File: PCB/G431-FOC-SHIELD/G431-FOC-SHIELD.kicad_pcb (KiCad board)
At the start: 2 copper layers, 70 x 59 mm, 2 parts, among them CN10 Conn_02x19_Odd_Even, CN7 Conn_02x19_Odd_Even

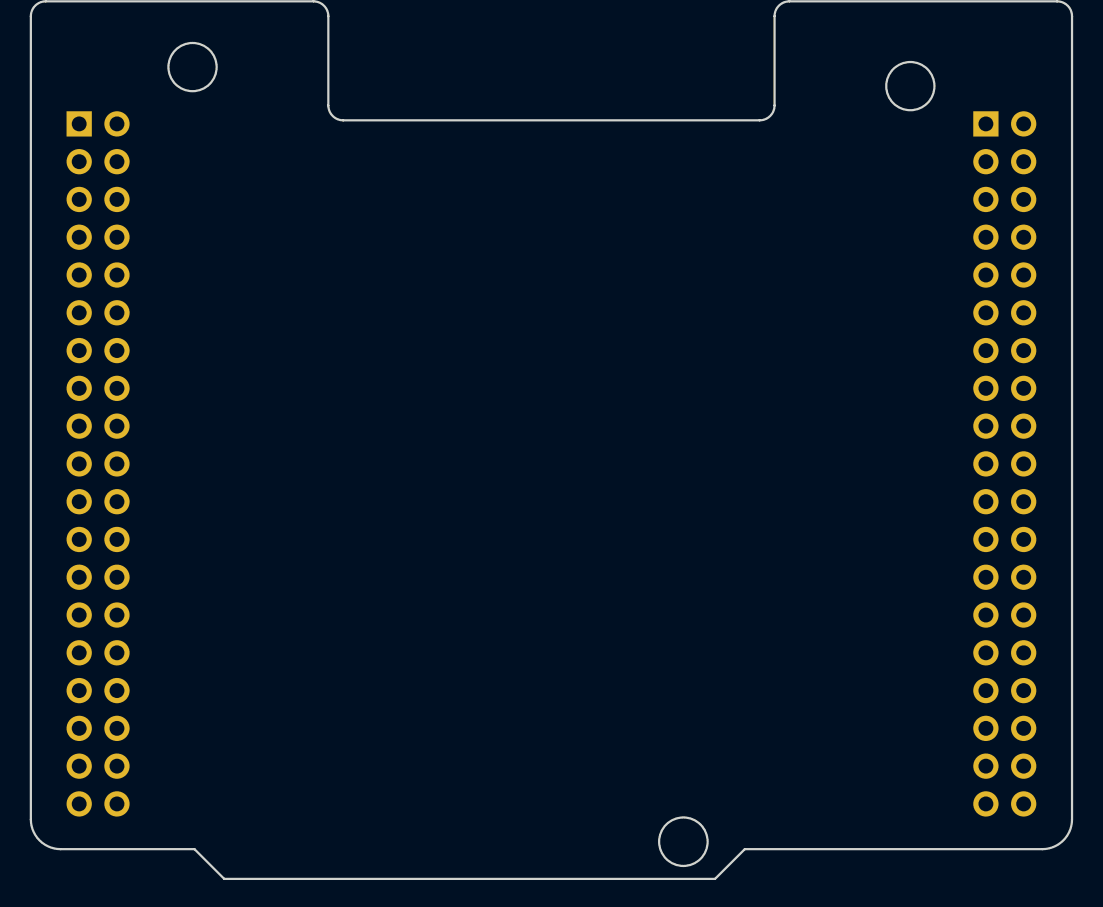
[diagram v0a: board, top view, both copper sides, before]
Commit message: started schematic design, added DRV8323 typical application
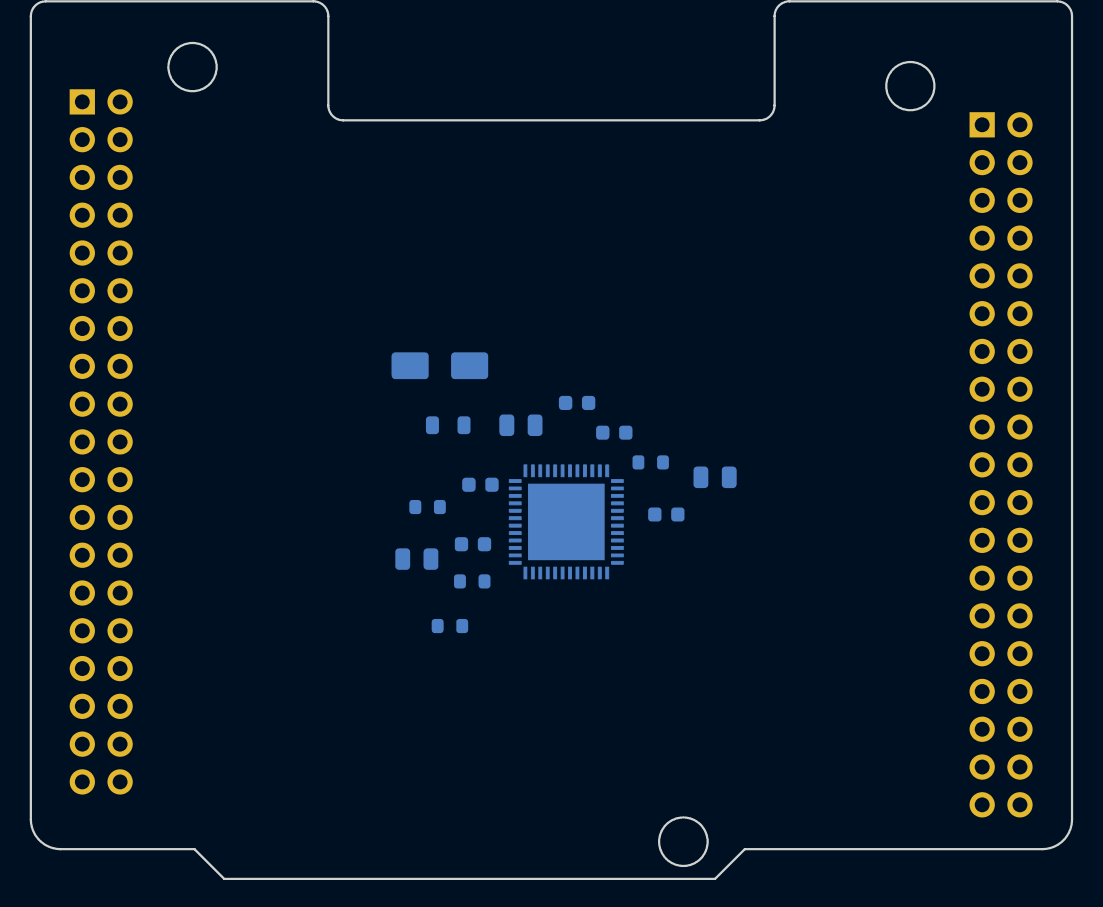
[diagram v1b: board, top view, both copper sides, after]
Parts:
- added C1: 0.1u, Capacitor_SMD:C_0603_1608Metric, B.Cu at (166.7, 90.0)
- added C2: Cin, Capacitor_SMD:C_0805_2012Metric, B.Cu at (162.9, 91.5)
- added C3: C_OUT, Capacitor_SMD:C_0805_2012Metric, B.Cu at (155.9, 100.5)
- added C4: 47u, Capacitor_SMD:C_0805_2012Metric, B.Cu at (176.0, 95.0)
- added C5: 1u, Capacitor_SMD:C_0603_1608Metric, B.Cu at (172.7, 97.5)
- added C6: 0.1u, Capacitor_SMD:C_0603_1608Metric, B.Cu at (169.2, 92.0)
- added C7: 1u, Capacitor_SMD:C_0603_1608Metric, B.Cu at (159.7, 99.5)
- added C8: 1u, Capacitor_SMD:C_0603_1608Metric, B.Cu at (160.2, 95.5)
- added D1: D_Schottky, Diode_SMD:D_SMA, B.Cu at (157.5, 87.5)
- added L1: L_OUT, Inductor_SMD:L_0805_2012Metric, B.Cu at (158.1, 91.5)
- added R1: R, Resistor_SMD:R_0603_1608Metric, B.Cu at (171.7, 94.0)
- added R2: R_FB_1, Resistor_SMD:R_0603_1608Metric, B.Cu at (159.7, 102.0)
- added R3: R_FB_2, Resistor_SMD:R_0603_1608Metric, B.Cu at (158.2, 105.0)
- added R4: 10k, Resistor_SMD:R_0603_1608Metric, B.Cu at (156.7, 97.0)
- added U1: DRV8323RSRGZR, DRV8323RSRGZR:QFN50P700X700X100-49N, B.Cu at (166.0, 98.0)
- moved CN7 1.49 mm to (133.5, 69.8)
- moved CN10 0.26 mm to (194.0, 71.3)
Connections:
- net Net-(CN10-Pad1) renamed /PC9
- net Net-(CN10-Pad11) renamed /PA5
- net Net-(CN10-Pad12) renamed /PA12
- net Net-(CN10-Pad13) renamed /PA6
- net Net-(CN10-Pad14) renamed /PA11
- net Net-(CN10-Pad15) renamed /PA7
- net Net-(CN10-Pad16) renamed /PB12
- net Net-(CN10-Pad17) renamed /PB6
- net Net-(CN10-Pad18) renamed /PB11
- net Net-(CN10-Pad19) renamed /PC7
- net Net-(CN10-Pad2) renamed /PC8
- net Net-(CN10-Pad21) renamed /PA9
- net Net-(CN10-Pad22) renamed /PB2
- net Net-(CN10-Pad23) renamed /PA8
- net Net-(CN10-Pad24) renamed /PB1
- net Net-(CN10-Pad25) renamed /PB10
- net Net-(CN10-Pad26) renamed /PB15
- net Net-(CN10-Pad27) renamed /PB4
- net Net-(CN10-Pad28) renamed /PB14
- net Net-(CN10-Pad29) renamed /PB5
- net Net-(CN10-Pad3) renamed /PB8
- net Net-(CN10-Pad30) renamed /PB13
- net Net-(CN10-Pad31) renamed /PB3
- net Net-(CN10-Pad32) renamed /AGND
- net Net-(CN10-Pad33) renamed /PA10
- net Net-(CN10-Pad34) renamed /PC4
- net Net-(CN10-Pad35) renamed /PC4/PA2
- net Net-(CN10-Pad37) renamed /PC5/PA3
- net Net-(CN10-Pad4) renamed /PC6
- net Net-(CN10-Pad5) renamed /PB9
- net Net-(CN10-Pad6) renamed /PC5
- net Net-(CN10-Pad7) renamed /AVDD
- net Net-(CN10-Pad8) renamed /5V_USB_CHGR
- net Net-(CN7-Pad1) renamed /PC10
- net Net-(CN7-Pad12) renamed /IOREF
- net Net-(CN7-Pad13) renamed /PA13
- net Net-(CN7-Pad14) renamed /NRST
- net Net-(CN7-Pad15) renamed /PA14
- net Net-(CN7-Pad16) renamed /+3V3
- net Net-(CN7-Pad17) renamed /PA15
- net Net-(CN7-Pad18) renamed /+5V
- net Net-(CN7-Pad2) renamed /PC11
- net Net-(CN7-Pad21) renamed /PB7
- net Net-(CN7-Pad23) renamed /PC13
- net Net-(CN7-Pad24) renamed /VIN
- net Net-(CN7-Pad25) renamed /PC14
- net Net-(CN7-Pad27) renamed /PC15
- net Net-(CN7-Pad28) renamed /PA0
- net Net-(CN7-Pad29) renamed /PF0
- net Net-(CN7-Pad3) renamed /PC12
- net Net-(CN7-Pad30) renamed /PA1
- net Net-(CN7-Pad31) renamed /PF1
- net Net-(CN7-Pad32) renamed /PA4
- net Net-(CN7-Pad33) renamed /VBAT
- net Net-(CN7-Pad34) renamed /PB0
- net Net-(CN7-Pad35) renamed /PC2
- net Net-(CN7-Pad36) renamed /PC1/PB9
- net Net-(CN7-Pad37) renamed /PC3
- net Net-(CN7-Pad38) renamed /PC0/PA15
- net Net-(CN7-Pad4) renamed /PD2
- net Net-(CN7-Pad5) renamed /VDD
- net Net-(CN7-Pad6) renamed /E5V
- net Net-(CN7-Pad7) renamed /PB8-BOOT0
- CN10 pad 10: Net-(CN10-Pad10) -> unconnected-(CN10-Pin_10-Pad10)
- CN10 pad 20: Net-(CN10-Pad20) -> GND
- CN10 pad 36: Net-(CN10-Pad36) -> unconnected-(CN10-Pin_36-Pad36)
- CN10 pad 38: Net-(CN10-Pad38) -> unconnected-(CN10-Pin_38-Pad38)
- CN10 pad 9: Net-(CN10-Pad9) -> GND
- CN7 pad 10: Net-(CN7-Pad10) -> /NC
- CN7 pad 11: Net-(CN7-Pad11) -> /NC
- CN7 pad 19: Net-(CN7-Pad19) -> GND
- CN7 pad 20: Net-(CN7-Pad20) -> GND
- CN7 pad 22: Net-(CN7-Pad22) -> GND
- CN7 pad 26: Net-(CN7-Pad26) -> unconnected-(CN7-Pin_26-Pad26)
- CN7 pad 8: Net-(CN7-Pad8) -> GND
- CN7 pad 9: Net-(CN7-Pad9) -> /NC
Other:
- board text added: "FIX PLACEMENT OF HEADERS"
- board text added: "FOC-SHIELD"
- board text removed: "STM32 Morpho"

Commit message: calculations in schematic
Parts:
- added C10: C, Capacitor_SMD:C_0603_1608Metric, F.Cu at (175.0, 85.8)
- added C11: C, Capacitor_SMD:C_0603_1608Metric, F.Cu at (175.0, 88.3)
- added C9: C, Capacitor_SMD:C_0603_1608Metric, F.Cu at (1.50, 0.76)
- C1: value 0.1u -> 100n
- C2: value Cin -> 2.2u
- C3: value C_OUT -> 10u
- C4: value 47u -> 47n
- L1: value L_OUT -> 22uH
- R1: value R -> 100k
- R2: value R_FB_1 -> 331.4k
- R3: value R_FB_2 -> 100k
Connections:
- CN10 pad 12: /PA12 -> /INLB
- CN10 pad 21: /PA9 -> /INHB
- CN10 pad 23: /PA8 -> /INHA
- CN10 pad 24: /PB1 -> /INLC
- CN10 pad 26: /PB15 -> /ENABLE
- CN10 pad 30: /PB13 -> /INLA
- CN10 pad 33: /PA10 -> /INHC
- U1 pad 12: /SNA -> GND
- U1 pad 13: /SNB -> GND
- U1 pad 16: /SHB -> /A
- U1 pad 19: /SHC -> /A
- U1 pad 22: /SNC -> GND
- U1 pad 23: unconnected-(U1-SOC-Pad23) -> /PC2
- U1 pad 24: unconnected-(U1-SOB-Pad24) -> /PC1
- U1 pad 25: unconnected-(U1-SOA-Pad25) -> /PC0
- U1 pad 29: unconnected-(U1-SDO-Pad29) -> /PA6
- U1 pad 30: unconnected-(U1-SDI-Pad30) -> /PA7
- U1 pad 31: unconnected-(U1-SCLK-Pad31) -> /PA5
- U1 pad 32: unconnected-(U1-nSCS-Pad32) -> /PB12
- U1 pad 33: unconnected-(U1-ENABLE-Pad33) -> /ENABLE
- U1 pad 34: unconnected-(U1-CAL-Pad34) -> GND
- U1 pad 37: unconnected-(U1-INHA-Pad37) -> /INHA
- U1 pad 38: unconnected-(U1-INLA-Pad38) -> /INLA
- U1 pad 39: unconnected-(U1-INHB-Pad39) -> /INHB
- U1 pad 40: unconnected-(U1-INLB-Pad40) -> /INLB
- U1 pad 41: unconnected-(U1-INHC-Pad41) -> /INHC
- U1 pad 42: unconnected-(U1-INLC-Pad42) -> /INLC
- U1 pad 9: /SHA -> /A

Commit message: started layout
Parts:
- added C12: 4700u, Capacitor_THT:CP_Radial_D16.0mm_P7.50mm, F.Cu at (93.6, 52.8)
- added J1: Screw_Terminal_01x02, TerminalBlock_Phoenix:TerminalBlock_Phoenix_MKDS-1,5-2_1x02_P5.00mm_Horizontal, F.Cu at (140.5, 33.0)
- added J2: Screw_Terminal_01x03, TerminalBlock_Phoenix:TerminalBlock_Phoenix_MKDS-1,5-3_1x03_P5.00mm_Horizontal, F.Cu at (197.0, 33.5)
- added Q1: Q_NMOS_GDS, Package_TO_SOT_SMD:TO-263-3_TabPin2, F.Cu at (134.2, 49.5)
- added Q2: Q_NMOS_GDS, Package_TO_SOT_SMD:TO-263-3_TabPin2, F.Cu at (146.6, 49.5)
- added Q3: Q_NMOS_GDS, Package_TO_SOT_SMD:TO-263-3_TabPin2, F.Cu at (158.9, 49.5)
- added Q4: Q_NMOS_GDS, Package_TO_SOT_SMD:TO-263-3_TabPin2, F.Cu at (171.3, 49.5)
- added Q5: Q_NMOS_GDS, Package_TO_SOT_SMD:TO-263-3_TabPin2, F.Cu at (183.7, 49.5)
- added Q6: Q_NMOS_GDS, Package_TO_SOT_SMD:TO-263-3_TabPin2, F.Cu at (196.0, 49.5)
- added R5: 2m, Resistor_SMD:R_2512_6332Metric, F.Cu at (100.5, 64.0)
- added R6: 2m, Resistor_SMD:R_2512_6332Metric, F.Cu at (100.5, 68.9)
- added R7: 2m, Resistor_SMD:R_2512_6332Metric, F.Cu at (100.5, 73.8)
- added R8: 100k, Resistor_SMD:R_0603_1608Metric, F.Cu at (94.1, 70.3)
- added R9: 10k, Resistor_SMD:R_0603_1608Metric, F.Cu at (94.1, 72.8)
- C1, C2, C3, C4, C5, C6, C7, C8, D1, R1, R2, R3, R4, U1: moved to F.Cu
- C10, C11, C9: value C -> 4.7u; footprint Capacitor_SMD:C_0603_1608Metric -> Capacitor_SMD:C_1210_3225Metric
- L1: footprint Inductor_SMD:L_0805_2012Metric -> Inductor_SMD:L_1210_3225Metric; moved to F.Cu
- moved C9 118.7 mm to (90.9, 78.7)
- moved C5 88.7 mm to (90.1, 65.3), turned to 0 degrees
- moved C4 85.7 mm to (90.3, 96.9), turned to 0 degrees
- moved C10 84.1 mm to (90.9, 83.0)
- moved C11 84.1 mm to (90.9, 87.2)
- moved R1 83.7 mm to (90.1, 75.4), turned to 0 degrees
- moved C6 82.7 mm to (90.1, 67.8), turned to 0 degrees
- moved C1 81.3 mm to (90.1, 62.8), turned to 0 degrees
- moved R2 76.4 mm to (94.1, 62.8), turned to 0 degrees
- moved C7 75.5 mm to (90.1, 70.3), turned to 0 degrees
- moved R3 75.3 mm to (94.1, 65.3), turned to 0 degrees
- moved C8 73.7 mm to (90.1, 72.8), turned to 0 degrees
- moved C2 72.6 mm to (90.3, 90.9), turned to 0 degrees
- moved R4 69.0 mm to (94.1, 67.8), turned to 0 degrees
- moved C3 65.9 mm to (90.3, 93.9), turned to 0 degrees
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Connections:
- U1 pad 16: /A -> /B
- U1 pad 19: /A -> /C
- U1 pad 49: (no net) -> GND
- U1 pad 7: /VDRAIN -> VM
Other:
- board size 70 x 59 mm -> 80 x 95 mm
- board text removed: "FIX PLACEMENT OF HEADERS"

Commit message: 4-layer stackup
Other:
- copper layers 2 -> 4
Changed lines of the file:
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@@
 	(layers
 		(0 "F.Cu" signal)
+		(4 "In1.Cu" signal)
+		(6 "In2.Cu" signal)
 		(2 "B.Cu" signal)
 		(9 "F.Adhes" user "F.Adhesive")
@@
 	)
 	(setup
+		(stackup
+			(layer "F.SilkS"
+				(type "Top Silk Screen")
+			)
+			(layer "F.Paste"
+				(type "Top Solder Paste")
+			)
+			(layer "F.Mask"
+				(type "Top Solder Mask")
+				(thickness 0.01)
+			)
+			(layer "F.Cu"
+				(type "copper")
+				(thickness 0.035)
+			)
+			(layer "dielectric 1"
+				(type "prepreg")
+				(thickness 0.1)
+				(material "FR4")
+				(epsilon_r 4.5)
+				(loss_tangent 0.02)
+			)
+			(layer "In1.Cu"
+				(type "copper")
+				(thickness 0.035)
+			)
+			(layer "dielectric 2"
+				(type "core")
+				(thickness 1.24)
+				(material "FR4")
+				(epsilon_r 4.5)
+				(loss_tangent 0.02)
+			)
+			(layer "In2.Cu"
+				(type "copper")
+				(thickness 0.035)
+			)
+			(layer "dielectric 3"
+				(type "prepreg")
+				(thickness 0.1)
+				(material "FR4")
+				(epsilon_r 4.5)
+				(loss_tangent 0.02)
+			)
+			(layer "B.Cu"
+				(type "copper")
+				(thickness 0.035)
+			)
+			(layer "B.Mask"
+				(type "Bottom Solder Mask")
+				(thickness 0.01)
+			)
+			(layer "B.Paste"
+				(type "Bottom Solder Paste")
+			)
+			(layer "B.SilkS"
+				(type "Bottom Silk Screen")
+			)
+			(copper_finish "None")
+			(dielectric_constraints no)
+		)
 		(pad_to_mask_clearance 0.2)
 		(allow_soldermask_bridges_in_footprints no)
@@
 		(capping no)
 		(filling no)
+		(zone_defaults)
 		(aux_axis_origin 130 120)
 		(grid_origin 130 120)

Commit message: started placement
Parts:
- moved C12 19.2 mm to (108.0, 40.0)
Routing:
- added copper zone on In1.Cu, net GND
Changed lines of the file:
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@@
 	(footprint "Capacitor_THT:CP_Radial_D16.0mm_P7.50mm"
 		(layer "F.Cu")
-		(at 93.609491 52.775)
+		(at 108 40)
 		(descr "CP, Radial series, Radial, pin pitch=7.50mm, diameter=16mm, height=25mm, Electrolytic Capacitor")
 		(tags "CP Radial series Radial pin pitch 7.50mm diameter 16mm height 25mm Electrolytic Capacitor")
@@
 		)
 	)
+	(zone
+		(net "GND")
+		(layer "In1.Cu")
+		(name "GND")
+		(hatch edge 0.5)
+		(connect_pads
+			(clearance 0.508)
+		)
+		(min_thickness 0.25)
+		(fill
+			(thermal_gap 0.5)
+			(thermal_bridge_width 0.5)
+			(island_removal_mode 0)
+		)
+		(polygon
+			(pts
+				(xy 124.658226 122.390289) (xy 124.911264 27.039699) (xy 208.031344 26.637534) (xy 207.45894 122.610022)
+			)
+		)
+	)
